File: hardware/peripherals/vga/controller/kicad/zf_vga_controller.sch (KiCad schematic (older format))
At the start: 13 parts, among them J1 Conn_01x09, Q1 BC547, SW1 SW_Push_Dual, SW2 SW_Push_Dual, SW3 SW_Push_Dual, SW4 SW_Push_Dual, SW5 SW_Push_Dual, SW6 SW_Push_Dual, U1 74HC541

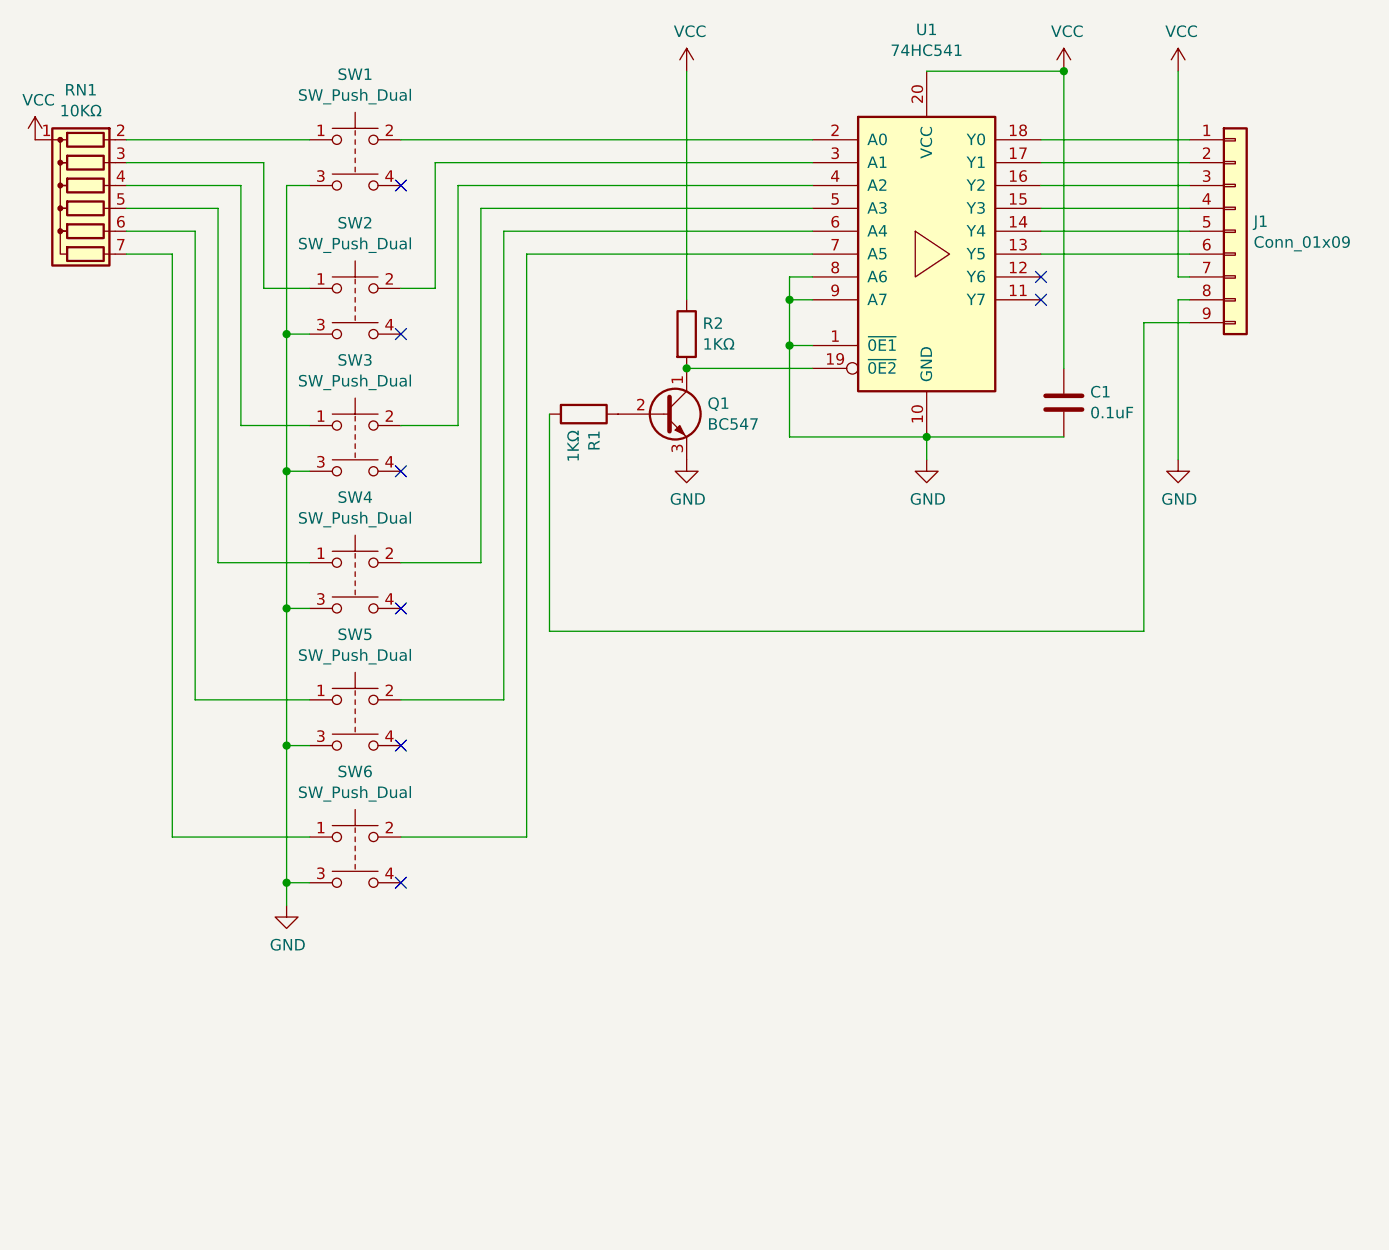
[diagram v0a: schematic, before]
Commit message: Redesigned controller around '241 buffer, added 2 extra buttons, increased height of PCB, added DE-9 connector
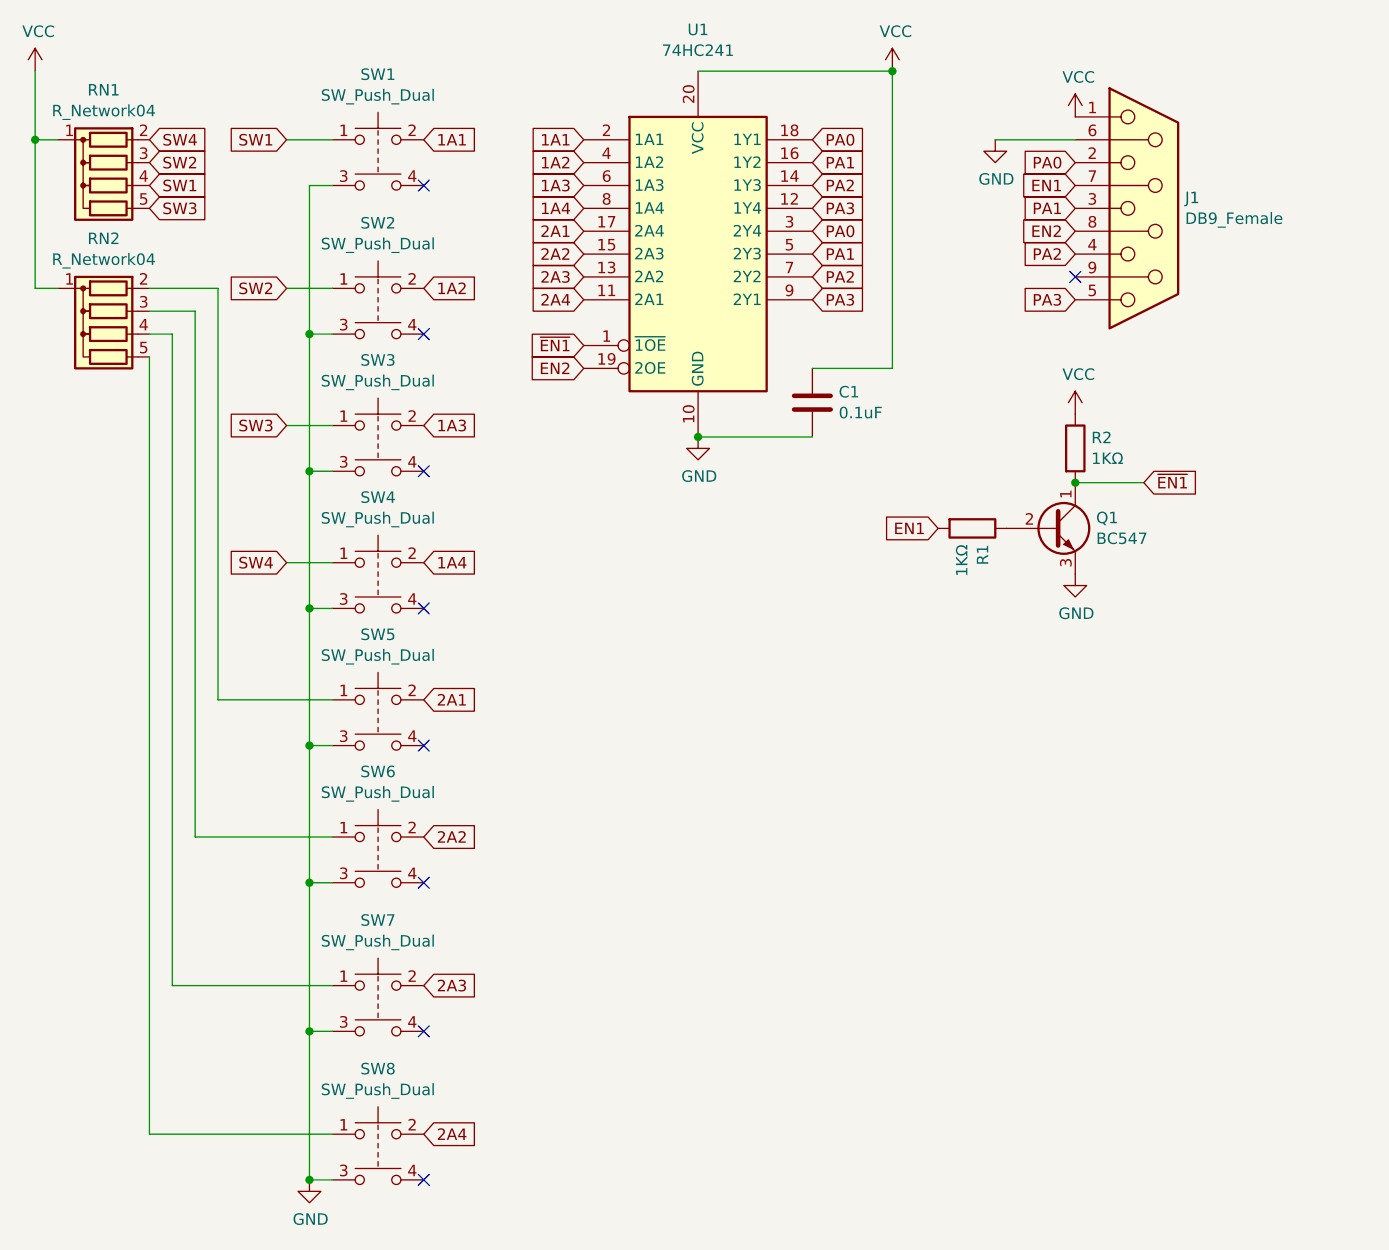
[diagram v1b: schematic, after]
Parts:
- removed J1: Conn_01x09, Connector_PinHeader_2.54mm:PinHeader_1x09_P2.54mm_Vertical, symbol Connector_Generic:Conn_01x09
- removed RN1: 10KΩ, Resistor_THT:R_Array_SIP7, symbol Device:R_Network06
- removed U1: 74HC541, Package_DIP:DIP-20_W7.62mm_LongPads, symbol 74xx:74HC541
- added J1: DB9_Female, Connector_Dsub:DSUB-9_Female_Horizontal_P2.77x2.84mm_EdgePinOffset7.70mm_Housed_MountingHolesOffset9.12mm, symbol Connector:DB9_Female
- added RN1, RN2: R_Network04, Resistor_THT:R_Array_SIP5, symbol Device:R_Network04
- added SW7, SW8: SW_Push_Dual, zf_vga_controller:SW_B3F-4050, symbol Switch:SW_Push_Dual
- added U1: 74HC241, Package_DIP:DIP-20_W7.62mm, symbol 74xx:74HC241
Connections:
- net GND: now also J1.6, SW7.3, SW8.3, U1.10 (GND)
- net VCC: now also J1.1, RN1.1 (common), RN2.1 (common), U1.20 (VCC)
- net SW1: now reaches SW1.1
- net SW1: now also RN1.4 (R3)
- net 1A1: now reaches SW1.2
- net 1A1: now also U1.2 (1A1)
- net SW3: now reaches SW3.1
- net SW3: now also RN1.5 (R4)
- net 1A3: now reaches SW3.2
- net 1A3: now also U1.6 (1A3)
- net SW4: now reaches SW4.1
- net SW4: now also RN1.2 (R1)
- net 1A4: now reaches SW4.2
- net 1A4: now also U1.8 (1A4)
- net SW2: now reaches SW2.1
- net SW2: now also RN1.3 (R2)
- net 1A2: now reaches SW2.2
- net 1A2: now also U1.4 (1A2)
- net at SW5.1: now also RN2.2 (R1)
- net 2A1: now reaches SW5.2
- net 2A1: now also U1.17 (2A4)
- net at SW6.1: now also RN2.3 (R2)
- net 2A2: now reaches SW6.2
- net 2A2: now also U1.15 (2A3)
- net EN1: now reaches R1.2
- net EN1: now also J1.7
- net ~EN1: now reaches Q1.1 (C), R2.2
- net ~EN1: now also U1.1 (~1OE)
- new net: RN2.4 (R3), SW7.1
- new net: RN2.5 (R4), SW8.1
- new net 2A3: SW7.2, U1.13 (2A2)
- new net 2A4: SW8.2, U1.11 (2A1)
- new net EN2: J1.8, U1.19 (2OE)
- new net PA0: J1.2, U1.18 (1Y1), U1.3 (2Y4)
- new net PA1: J1.3, U1.16 (1Y2), U1.5 (2Y3)
- new net PA2: J1.4, U1.14 (1Y3), U1.7 (2Y2)
- new net PA3: J1.5, U1.12 (1Y4), U1.9 (2Y1)
- no-connect marks 8 -> 9
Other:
- moved on the sheet: C1, SW1, SW2, SW3, SW4, SW5, SW6

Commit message: Schematic media, fixes
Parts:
- RN1, RN2: value R_Network04 -> 10KΩ
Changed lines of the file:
@@
 P 950 1350
 F 0 "RN1" V 533 1350 50  0000 C CNN
-F 1 "R_Network04" V 624 1350 50  0000 C CNN
+F 1 "10KΩ" V 624 1350 50  0000 C CNN
 F 2 "Resistor_THT:R_Array_SIP5" V 1225 1350 50  0001 C CNN
 F 3 "http://www.vishay.com/docs/31509/csc.pdf" H 950 1350 50  0001 C CNN
@@
 P 950 2000
 F 0 "RN2" V 533 2000 50  0000 C CNN
-F 1 "R_Network04" V 624 2000 50  0000 C CNN
+F 1 "10KΩ" V 624 2000 50  0000 C CNN
 F 2 "Resistor_THT:R_Array_SIP5" V 1225 2000 50  0001 C CNN
 F 3 "http://www.vishay.com/docs/31509/csc.pdf" H 950 2000 50  0001 C CNN
